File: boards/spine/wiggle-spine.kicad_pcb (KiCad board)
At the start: 2 copper layers, 114.3 x 88.9 mm, 187 parts, among them CON1 USB-B, CON2 XLR-3 Female, CON3 USB-A, CON4 2.5mm 5-24V 5A, CON5 5-24V 16A, CON6 PLR135, CON7 PLT133, Q1 DMN3190LDW, Q2 2N7002P, Q3 AOD4189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

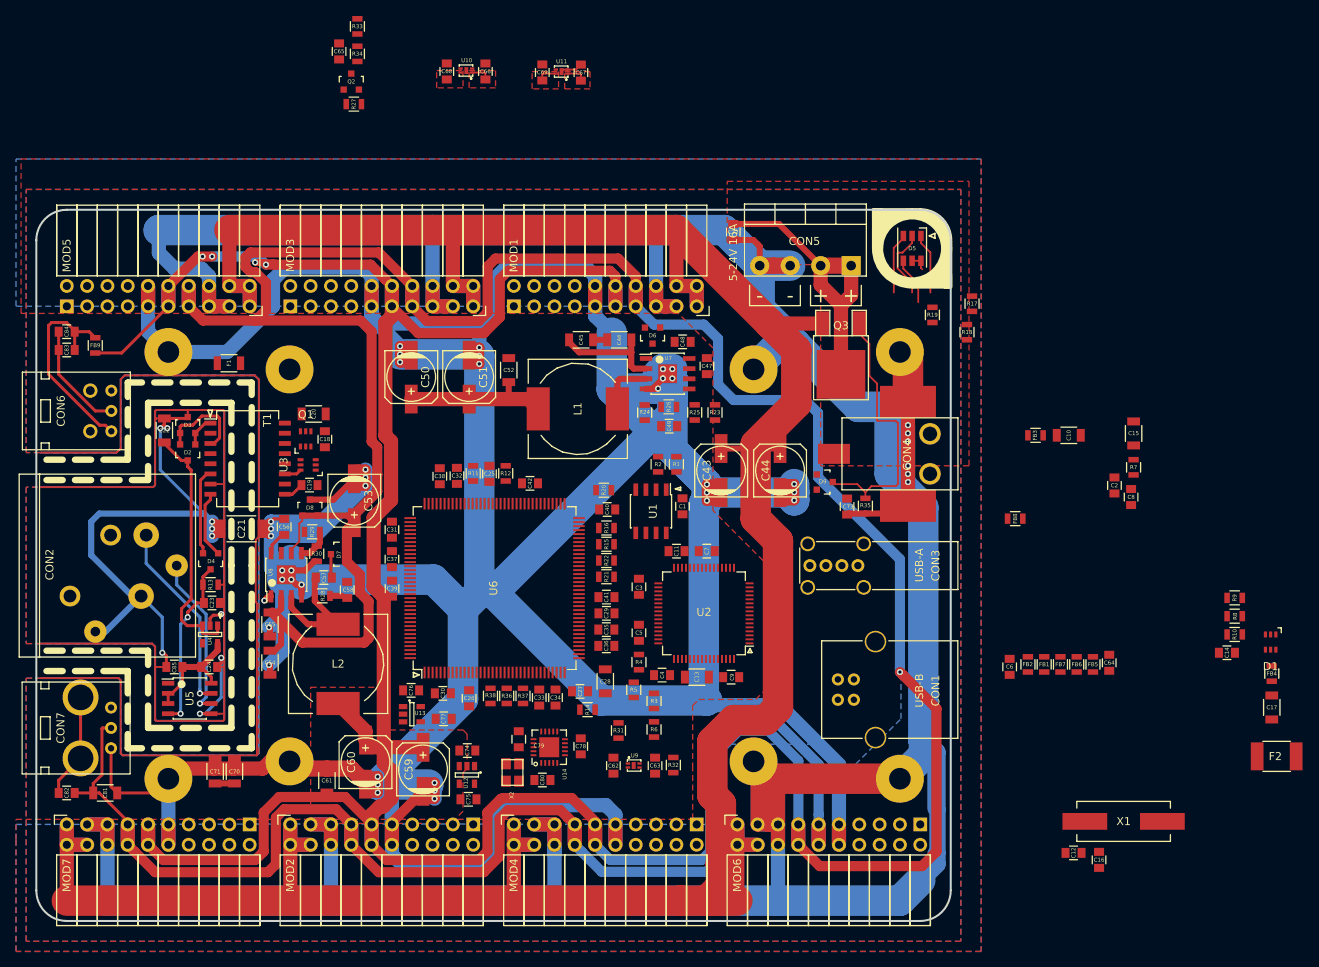
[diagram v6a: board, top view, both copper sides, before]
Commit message: Redo component annotation
Noticed the module numbers were wrong after the last reannotation, so this seemed like a good time to reannotate again.
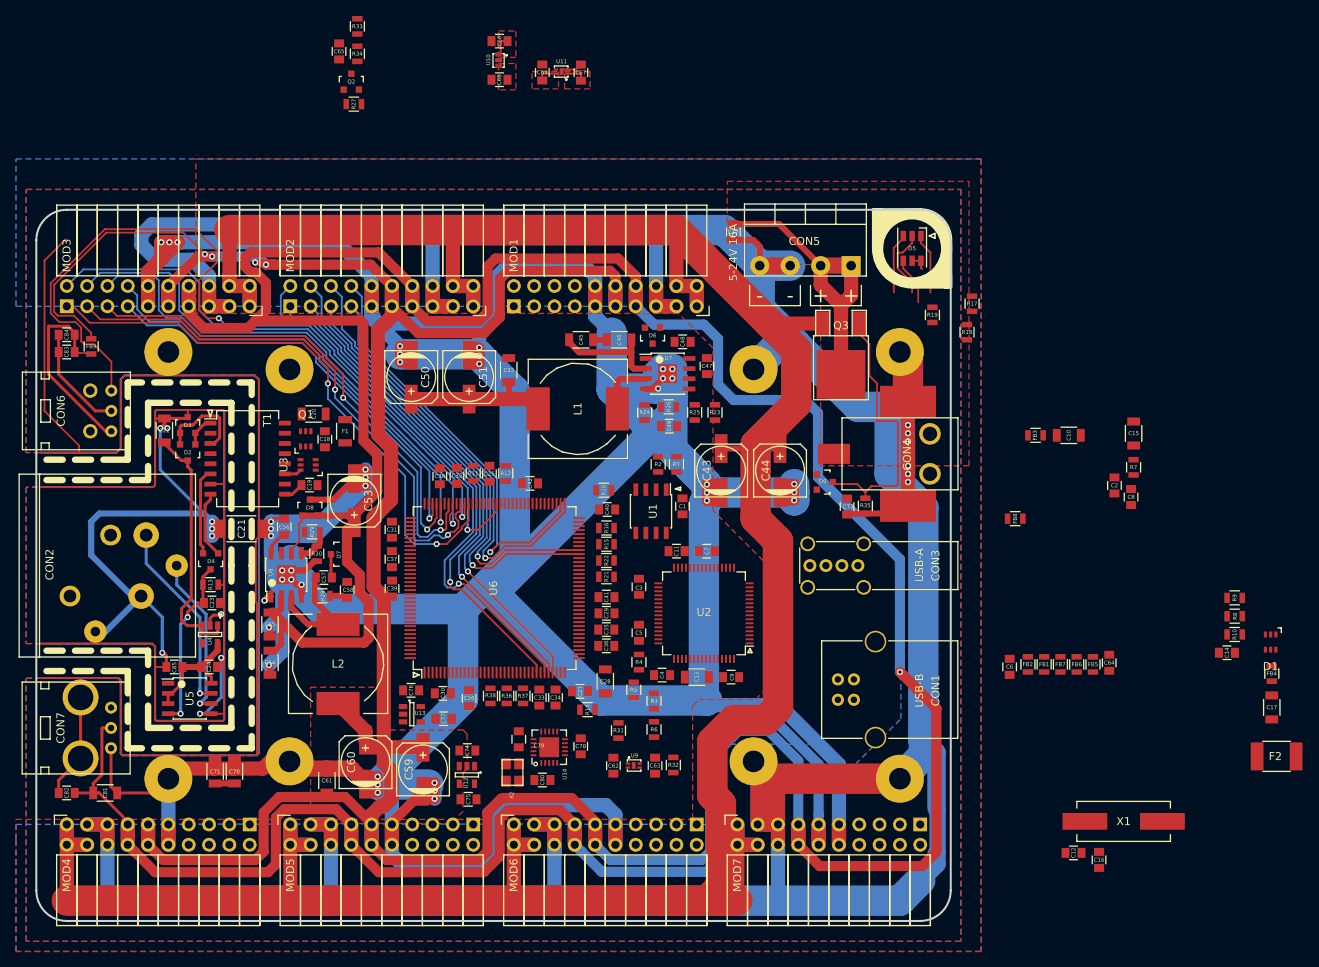
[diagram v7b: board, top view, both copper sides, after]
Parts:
- moved F1 16.8 mm to (123.7, 69.6), turned to 90 degrees
- moved C68 6.67 mm to (143.0, 25.7), turned to 0 degrees
- moved U10 4.23 mm to (142.9, 23.2), turned to 180 degrees
- moved C66 4.18 mm to (143.0, 20.8), turned to 180 degrees
- moved FB9 0.52 mm to (91.9, 59.0), turned to 270 degrees
- moved C84 0.38 mm to (88.9, 57.5)
- moved C83 0.25 mm to (88.9, 59.7)
- renumbered MOD3 to MOD2, MOD5 to MOD3, MOD7 to MOD4, MOD2 to MOD5, MOD4 to MOD6, MOD6 to MOD7
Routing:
- net /Sync In/Out/RXD: track 0.00 -> 105.7 mm, vias 0 -> 2
- net MOD3_PIN1: track 0.00 -> 72.5 mm, vias 0 -> 2
- net MOD3_PIN3: track 0.00 -> 69.5 mm, vias 0 -> 2
- net MOD3_PIN2: track 0.00 -> 69.4 mm, vias 0 -> 1
- net MOD2_PIN2: track 0.00 -> 68.9 mm, vias 0 -> 1
- net MOD3_PIN4: track 0.00 -> 67.5 mm, vias 0 -> 1
- net MOD3_PIN5: track 0.00 -> 64.3 mm, vias 0 -> 2
- net MOD2_PIN1: track 0.00 -> 63.1 mm, vias 0 -> 1
- net MOD3_PIN6: track 0.00 -> 63.1 mm, vias 0 -> 1
- net MOD2_PIN4: track 0.00 -> 62.8 mm, vias 0 -> 1
- net MOD2_PIN3: track 0.00 -> 60.3 mm, vias 0 -> 1
- net MOD3_PIN7: track 0.00 -> 57.2 mm, vias 0 -> 1
- net MOD2_PIN6: track 0.00 -> 56.8 mm, vias 0 -> 1
- net MOD3_PIN8: track 0.00 -> 56.7 mm, vias 0 -> 1
- net MOD2_PIN5: track 0.00 -> 55.6 mm, vias 0 -> 1
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
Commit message: Route some port GPIOs
but let's not get too carried away before placing everything...
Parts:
- moved C66 50.2 mm to (136.4, 70.6), turned to 90 degrees
- moved U10 48.1 mm to (134.0, 70.5), turned to 90 degrees
- moved C68 46.4 mm to (131.6, 70.6), turned to 270 degrees
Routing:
- net MOD4_PIN8: track 0.00 -> 71.8 mm, vias 0 -> 1
- net MOD4_PIN7: track 0.00 -> 67.5 mm, vias 0 -> 1
- net MOD4_PIN4: track 0.00 -> 66.6 mm, vias 0 -> 1
- net MOD4_PIN6: track 0.00 -> 66.0 mm, vias 0 -> 1
- net MOD4_PIN5: track 0.00 -> 63.3 mm, vias 0 -> 1
- net GND: track 1004.9 -> 1067.9 mm
- net MOD4_PIN3: track 0.00 -> 61.0 mm, vias 0 -> 1
- net MOD5_PIN8: track 0.00 -> 56.0 mm, vias 0 -> 1
- net MOD4_PIN2: track 0.00 -> 55.1 mm, vias 0 -> 1
- net MOD4_PIN1: track 0.00 -> 52.1 mm, vias 0 -> 1
- net MOD5_PIN7: track 0.00 -> 50.7 mm, vias 0 -> 1
- net MOD1_PIN8: track 0.00 -> 40.1 mm, vias 0 -> 1
- net MOD1_PIN3: track 0.00 -> 38.4 mm, vias 0 -> 1
- net MOD1_PIN4: track 0.00 -> 36.9 mm, vias 0 -> 1
- net MOD1_PIN2: track 0.00 -> 34.5 mm, vias 0 -> 1
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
